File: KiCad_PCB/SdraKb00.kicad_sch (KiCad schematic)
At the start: 75 parts, among them J2 AVR-ISP-6, SW03 RotaryEncoder_Switch, SW1 Reset_SW, U2 PRTR5V0U2X, U3 ATmega32U4-A, Y1 16MHz

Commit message: First round assigning footprints.
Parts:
- C1, C10, C11, C12, C13, C14, C15, C16, C17, C18, C19, C2, C20, C3, C4, C5, C6, C7, C8, C9: footprint (none) -> Capacitor_SMD:C_0805_2012Metric_Pad1.18x1.45mm_HandSolder
- D00, D01, D02, D03, D10, D11, D12, D13, D20, D21, D22, D23: footprint (none) -> Diode_SMD:D_SOD-123
- D14, D15, D16, D17, D18, D4, D5, D6, D7, D8, D9: footprint LED_SMD:LED_SK6812MINI_PLCC4_3.5x3.5mm_P1.75mm -> (none)
- F1: footprint (none) -> Fuse:Fuse_1206_3216Metric_Pad1.42x1.75mm_HandSolder
- H1, H2, H3, H4: footprint (none) -> MountingHole:MountingHole_2mm
- J2: footprint (none) -> random-keyboard-parts:Reset_Pretty-Mask
- R1, R2, R3, R4, R5, R6, R7, R8, R9: footprint (none) -> Resistor_SMD:R_0805_2012Metric_Pad1.20x1.40mm_HandSolder
- SW1: footprint (none) -> Button_Switch_SMD:SW_SPST_SKQG_WithStem
- U2: footprint (none) -> random-keyboard-parts:SOT143B
- USB1: footprint (none) -> Type-C:HRO-TYPE-C-31-M-12-HandSoldering
- Y1: footprint (none) -> Crystal:Crystal_SMD_3225-4Pin_3.2x2.5mm_HandSoldering
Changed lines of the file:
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@@
 			)
 		)
-		(property "Footprint" "LED_SMD:LED_SK6812MINI_PLCC4_3.5x3.5mm_P1.75mm"
+		(property "Footprint" ""
 			(at 332.74 113.03 0)
 			(effects
@@
 			)
 		)
-		(property "Footprint" ""
+		(property "Footprint" "MountingHole:MountingHole_2mm"
 			(at 135.89 149.86 0)
 			(effects
@@
 			)
 		)
-		(property "Footprint" "LED_SMD:LED_SK6812MINI_PLCC4_3.5x3.5mm_P1.75mm"
+		(property "Footprint" ""
 			(at 332.74 44.45 0)
 			(effects
@@
 			)
 		)
-		(property "Footprint" ""
+		(property "Footprint" "MountingHole:MountingHole_2mm"
 			(at 135.89 162.56 0)
 			(effects
@@
 			)
 		)
-		(property "Footprint" "LED_SMD:LED_SK6812MINI_PLCC4_3.5x3.5mm_P1.75mm"
+		(property "Footprint" ""
 			(at 360.68 78.74 0)
 			(effects
@@
 			)
 		)
-		(property "Footprint" ""
+		(property "Footprint" "Capacitor_SMD:C_0805_2012Metric_Pad1.18x1.45mm_HandSolder"
 			(at 123.19 114.3 0)
 			(effects
@@
 			)
 		)
-		(property "Footprint" ""
+		(property "Footprint" "MountingHole:MountingHole_2mm"
 			(at 158.75 149.86 0)
 			(effects
@@
 			)
 		)
-		(property "Footprint" ""
+		(property "Footprint" "Capacitor_SMD:C_0805_2012Metric_Pad1.18x1.45mm_HandSolder"
 			(at 295.91 67.31 0)
 			(effects
@@
 			)
 		)
-		(property "Footprint" ""
+		(property "Footprint" "Capacitor_SMD:C_0805_2012Metric_Pad1.18x1.45mm_HandSolder"
 			(at 295.91 101.6 0)
 			(effects
@@
 			)
 		)
-		(property "Footprint" ""
+		(property "Footprint" "Diode_SMD:D_SOD-123"
 			(at 172.72 48.26 90)
 			(effects
@@
 			)
 		)
-		(property "Footprint" ""
+		(property "Footprint" "Diode_SMD:D_SOD-123"
 			(at 123.19 48.26 90)
 			(effects
@@
 			)
 		)
-		(property "Footprint" ""
+		(property "Footprint" "Resistor_SMD:R_0805_2012Metric_Pad1.20x1.40mm_HandSolder"
 			(at 204.47 40.64 0)
 			(effects
@@
 			)
 		)
-		(property "Footprint" ""
+		(property "Footprint" "random-keyboard-parts:SOT143B"
 			(at 90.17 175.26 0)
 			(effects
@@
 			)
 		)
-		(property "Footprint" ""
+		(property "Footprint" "Diode_SMD:D_SOD-123"
 			(at 123.19 88.9 90)
 			(effects
@@
 			)
 		)
-		(property "Footprint" ""
+		(property "Footprint" "Fuse:Fuse_1206_3216Metric_Pad1.42x1.75mm_HandSolder"
 			(at 91.44 149.86 0)
 			(effects
@@
 			)
 		)
-		(property "Footprint" ""
+		(property "Footprint" "Type-C:HRO-TYPE-C-31-M-12-HandSoldering"
 			(at 45.72 162.56 0)
 			(effects
@@
 			)
 		)
-		(property "Footprint" ""
+		(property "Footprint" "Capacitor_SMD:C_0805_2012Metric_Pad1.18x1.45mm_HandSolder"
 			(at 323.85 67.31 0)
 			(effects
@@
 			)
 		)
-		(property "Footprint" ""
+		(property "Footprint" "Diode_SMD:D_SOD-123"
 			(at 139.7 88.9 90)
 			(effects
@@
 			)
 		)
-		(property "Footprint" "LED_SMD:LED_SK6812MINI_PLCC4_3.5x3.5mm_P1.75mm"
+		(property "Footprint" ""
 			(at 360.68 113.03 0)
 			(effects
@@
 			)
 		)
-		(property "Footprint" ""
+		(property "Footprint" "Capacitor_SMD:C_0805_2012Metric_Pad1.18x1.45mm_HandSolder"
 			(at 267.97 33.02 0)
 			(effects
@@
 			)
 		)
-		(property "Footprint" ""
+		(property "Footprint" "Capacitor_SMD:C_0805_2012Metric_Pad1.18x1.45mm_HandSolder"
 			(at 267.97 67.31 0)
 			(effects
@@
 			)
 		)
-		(property "Footprint" "LED_SMD:LED_SK6812MINI_PLCC4_3.5x3.5mm_P1.75mm"
+		(property "Footprint" ""
 			(at 332.74 78.74 0)
 			(effects
@@
 			)
 		)
-		(property "Footprint" ""
+		(property "Footprint" "Capacitor_SMD:C_0805_2012Metric_Pad1.18x1.45mm_HandSolder"
 			(at 154.94 124.46 0)
 			(effects
@@
 			)
 		)
-		(property "Footprint" ""
+		(property "Footprint" "random-keyboard-parts:Reset_Pretty-Mask"
 			(at 201.93 119.38 90)
 			(effects
@@
 			)
 		)
-		(property "Footprint" "LED_SMD:LED_SK6812MINI_PLCC4_3.5x3.5mm_P1.75mm"
+		(property "Footprint" ""
 			(at 304.8 44.45 0)
 			(effects
@@
 			)
 		)
-		(property "Footprint" "LED_SMD:LED_SK6812MINI_PLCC4_3.5x3.5mm_P1.75mm"
+		(property "Footprint" ""
 			(at 276.86 78.74 0)
 			(effects
@@
 			)
 		)
-		(property "Footprint" ""
+		(property "Footprint" "Diode_SMD:D_SOD-123"
 			(at 172.72 88.9 90)
 			(effects
@@
 			)
 		)
-		(property "Footprint" "LED_SMD:LED_SK6812MINI_PLCC4_3.5x3.5mm_P1.75mm"
+		(property "Footprint" ""
 			(at 304.8 113.03 0)
 			(effects
@@
 			)
 		)
-		(property "Footprint" ""
+		(property "Footprint" "Capacitor_SMD:C_0805_2012Metric_Pad1.18x1.45mm_HandSolder"
 			(at 323.85 33.02 0)
 			(effects
@@
 			)
 		)
-		(property "Footprint" ""
+		(property "Footprint" "Capacitor_SMD:C_0805_2012Metric_Pad1.18x1.45mm_HandSolder"
 			(at 213.36 38.1 0)
 			(effects
@@
 			)
 		)
-		(property "Footprint" ""
+		(property "Footprint" "Capacitor_SMD:C_0805_2012Metric_Pad1.18x1.45mm_HandSolder"
 			(at 351.79 101.6 0)
 			(effects
@@
 			)
 		)
-		(property "Footprint" ""
+		(property "Footprint" "Resistor_SMD:R_0805_2012Metric_Pad1.20x1.40mm_HandSolder"
 			(at 204.47 156.21 0)
 			(effects
@@
 			)
 		)
-		(property "Footprint" ""
+		(property "Footprint" "Capacitor_SMD:C_0805_2012Metric_Pad1.18x1.45mm_HandSolder"
 			(at 100.33 114.3 0)
 			(effects
@@
 			)
 		)
-		(property "Footprint" ""
+		(property "Footprint" "Resistor_SMD:R_0805_2012Metric_Pad1.20x1.40mm_HandSolder"
 			(at 204.47 45.72 0)
 			(effects
@@
 			)
 		)
-		(property "Footprint" ""
+		(property "Footprint" "Capacitor_SMD:C_0805_2012Metric_Pad1.18x1.45mm_HandSolder"
 			(at 31.75 72.39 0)
 			(effects
@@
 			)
 		)
-		(property "Footprint" ""
+		(property "Footprint" "Capacitor_SMD:C_0805_2012Metric_Pad1.18x1.45mm_HandSolder"
 			(at 135.89 114.3 0)
 			(effects
@@
 			)
 		)
-		(property "Footprint" ""
+		(property "Footprint" "Diode_SMD:D_SOD-123"
 			(at 123.19 68.58 90)
 			(effects
@@
 			)
 		)
-		(property "Footprint" ""
+		(property "Footprint" "Capacitor_SMD:C_0805_2012Metric_Pad1.18x1.45mm_HandSolder"
 			(at 213.36 48.26 0)
 			(effects
@@
 			)
 		)
-		(property "Footprint" "LED_SMD:LED_SK6812MINI_PLCC4_3.5x3.5mm_P1.75mm"
+		(property "Footprint" ""
 			(at 304.8 78.74 0)
 			(effects
@@
 			)
 		)
-		(property "Footprint" ""
+		(property "Footprint" "Capacitor_SMD:C_0805_2012Metric_Pad1.18x1.45mm_HandSolder"
 			(at 351.79 67.31 0)
 			(effects
@@
 			)
 		)
-		(property "Footprint" ""
+		(property "Footprint" "Diode_SMD:D_SOD-123"
 			(at 139.7 48.26 90)
 			(effects
@@
 			)
 		)
-		(property "Footprint" ""
+		(property "Footprint" "Diode_SMD:D_SOD-123"
 			(at 156.21 88.9 90)
 			(effects
@@
 			)
 		)
-		(property "Footprint" ""
+		(property "Footprint" "Capacitor_SMD:C_0805_2012Metric_Pad1.18x1.45mm_HandSolder"
 			(at 111.76 114.3 0)
 			(effects
@@
 			)
 		)
-		(property "Footprint" ""
+		(property "Footprint" "Resistor_SMD:R_0805_2012Metric_Pad1.20x1.40mm_HandSolder"
 			(at 81.28 90.17 0)
 			(effects
@@
 			)
 		)
-		(property "Footprint" ""
+		(property "Footprint" "Capacitor_SMD:C_0805_2012Metric_Pad1.18x1.45mm_HandSolder"
 			(at 295.91 33.02 0)
 			(effects
@@
 			)
 		)
-		(property "Footprint" ""
+		(property "Footprint" "Resistor_SMD:R_0805_2012Metric_Pad1.20x1.40mm_HandSolder"
 			(at 66.04 173.99 0)
 			(effects
@@
 			)
 		)
-		(property "Footprint" "LED_SMD:LED_SK6812MINI_PLCC4_3.5x3.5mm_P1.75mm"
+		(property "Footprint" ""
 			(at 276.86 113.03 0)
 			(effects
@@
 			)
 		)
-		(property "Footprint" ""
+		(property "Footprint" "Resistor_SMD:R_0805_2012Metric_Pad1.20x1.40mm_HandSolder"
 			(at 104.14 163.83 0)
 			(effects
@@
 			)
 		)
-		(property "Footprint" ""
+		(property "Footprint" "Diode_SMD:D_SOD-123"
 			(at 172.72 68.58 90)
 			(effects
@@
 			)
 		)
-		(property "Footprint" "LED_SMD:LED_SK6812MINI_PLCC4_3.5x3.5mm_P1.75mm"
+		(property "Footprint" ""
 			(at 276.86 44.45 0)
 			(effects
@@
 			)
 		)
-		(property "Footprint" ""
+		(property "Footprint" "Crystal:Crystal_SMD_3225-4Pin_3.2x2.5mm_HandSoldering"
 			(at 163.83 120.65 0)
 			(effects
@@
 			)
 		)
-		(property "Footprint" ""
+		(property "Footprint" "Capacitor_SMD:C_0805_2012Metric_Pad1.18x1.45mm_HandSolder"
 			(at 171.45 124.46 0)
 			(effects
@@
 			)
 		)
-		(property "Footprint" ""
+		(property "Footprint" "Capacitor_SMD:C_0805_2012Metric_Pad1.18x1.45mm_HandSolder"
 			(at 323.85 101.6 0)
 			(effects
@@
 			)
 		)
-		(property "Footprint" ""
+		(property "Footprint" "Diode_SMD:D_SOD-123"
 			(at 139.7 68.58 90)
 			(effects
@@
 			)
 		)
-		(property "Footprint" ""
+		(property "Footprint" "Diode_SMD:D_SOD-123"
 			(at 156.21 68.58 90)
 			(effects
@@
 			)
 		)
-		(property "Footprint" ""
+		(property "Footprint" "Resistor_SMD:R_0805_2012Metric_Pad1.20x1.40mm_HandSolder"
 			(at 73.66 173.99 0)
 			(effects
@@
 			)
 		)
-		(property "Footprint" ""
+		(property "Footprint" "Capacitor_SMD:C_0805_2012Metric_Pad1.18x1.45mm_HandSolder"
 			(at 267.97 101.6 0)
 			(effects
@@
 			)
 		)
-		(property "Footprint" ""
+		(property "Footprint" "Resistor_SMD:R_0805_2012Metric_Pad1.20x1.40mm_HandSolder"
 			(at 104.14 166.37 0)
 			(effects
@@
 			)
 		)
-		(property "Footprint" ""
+		(property "Footprint" "Button_Switch_SMD:SW_SPST_SKQG_WithStem"
 			(at 196.85 156.21 0)
 			(effects
@@
 			)
 		)
-		(property "Footprint" ""
+		(property "Footprint" "Resistor_SMD:R_0805_2012Metric_Pad1.20x1.40mm_HandSolder"
 			(at 256.54 36.83 0)
 			(effects
@@
 			)
 		)
-		(property "Footprint" ""
+		(property "Footprint" "Diode_SMD:D_SOD-123"
 			(at 156.21 48.26 90)
 			(effects
@@
 			)
 		)
-		(property "Footprint" ""
+		(property "Footprint" "MountingHole:MountingHole_2mm"
 			(at 158.75 162.56 0)
 			(effects

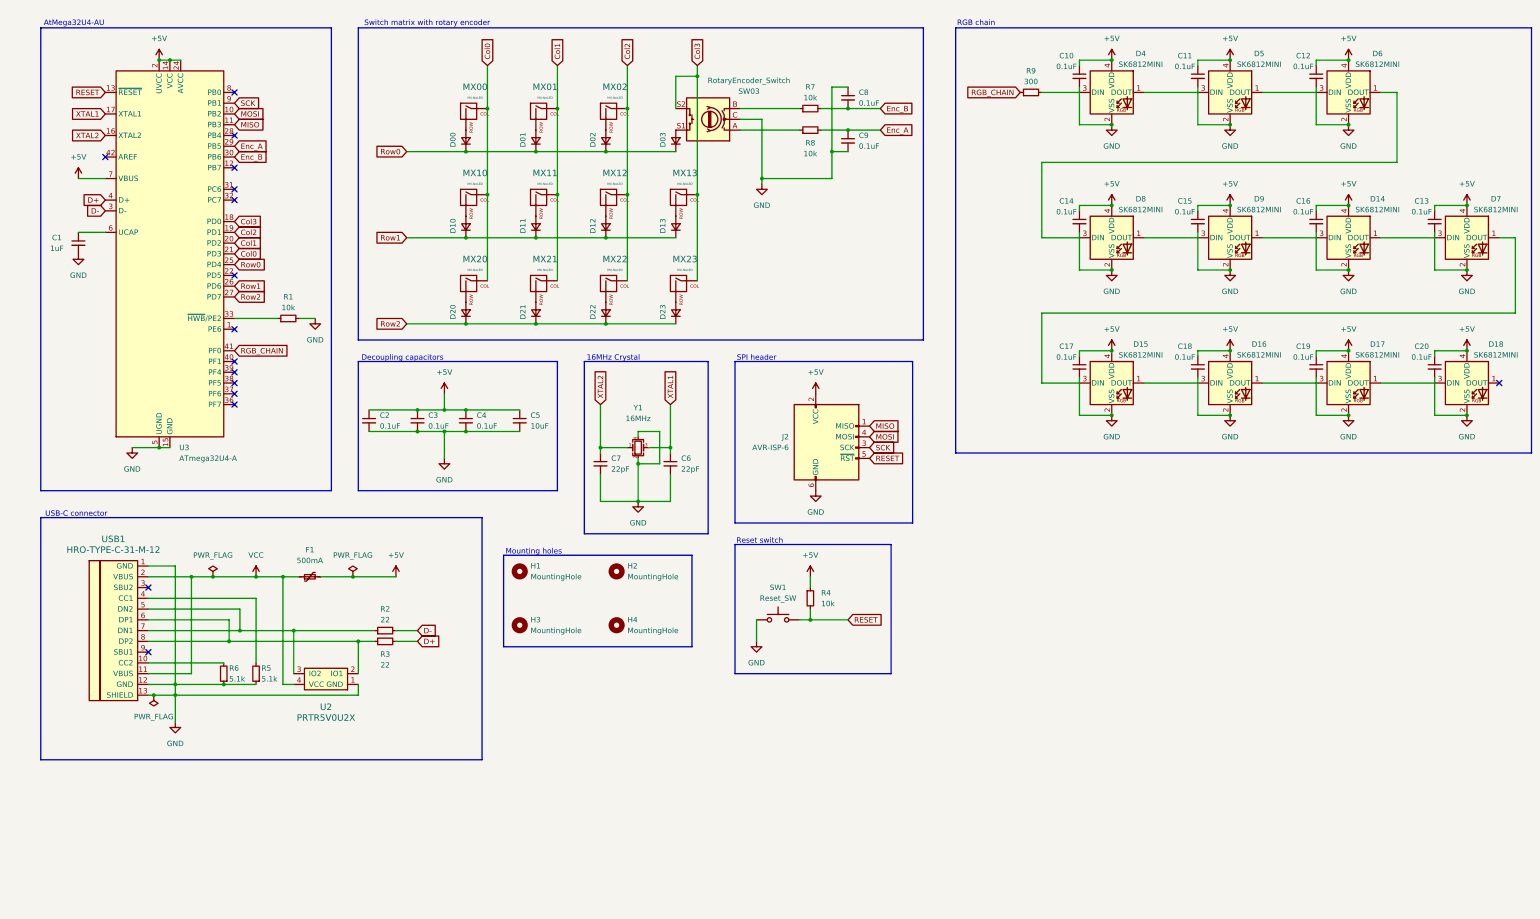
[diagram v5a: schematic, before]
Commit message: Complete footprint assignment.
- Removed unused submodules
- Adding marbastlib submodule
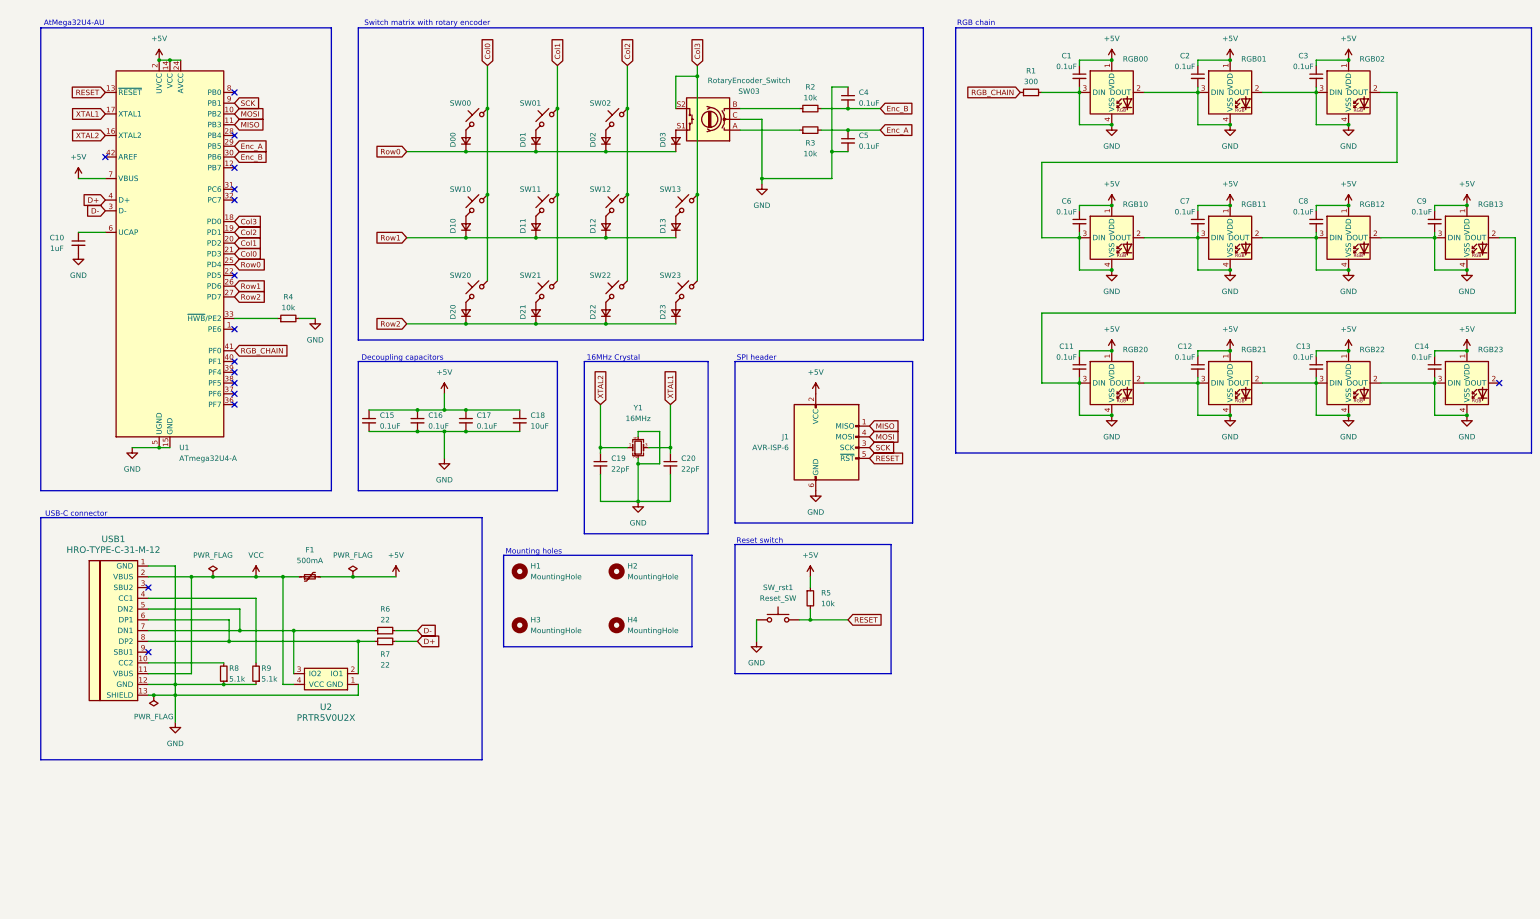
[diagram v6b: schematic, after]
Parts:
- removed D14, D15, D16, D17, D18, D4, D5, D6, D7, D8, D9: SK6812MINI, symbol LED:SK6812MINI
- removed MX00, MX01, MX02, MX10, MX11, MX12, MX13, MX20, MX21, MX22, MX23: MX-NoLED, symbol MX_Alps_Hybrid:MX-NoLED
- added RGB00, RGB01, RGB02, RGB10, RGB11, RGB12, RGB13, RGB20, RGB21, RGB22, RGB23: MX_SK6812MINI-E, marbastlib-mx:LED_MX_6028R, symbol marbastlib-mx:MX_SK6812MINI-E
- added SW00, SW01, SW02, SW10, SW11, SW12, SW13, SW20, SW21, SW22, SW23: SW_Push_45deg, marbastlib-mx:SW_MX_HS_CPG151101S11_1u, symbol Switch:SW_Push_45deg
- H1, H2, H3, H4: footprint MountingHole:MountingHole_2mm -> MountingHole:MountingHole_3.2mm_M3
- J1: renamed from J2; footprint random-keyboard-parts:Reset_Pretty-Mask -> Connector_IDC:IDC-Header_2x03_P2.54mm_Vertical
- SW03: footprint (none) -> marbastlib-various:ROT_Alps_EC11E-Switch
- U2: footprint random-keyboard-parts:SOT143B -> Package_TO_SOT_SMD:SOT-143_Handsoldering
- renumbered C10 to C1, C1 to C10, C17 to C11, C18 to C12, C19 to C13, C20 to C14, C2 to C15, C3 to C16, C4 to C17, C5 to C18, C7 to C19, C11 to C2, C6 to C20, C12 to C3, C8 to C4, C9 to C5, C14 to C6, C15 to C7, C16 to C8, C13 to C9, R9 to R1, R7 to R2, R8 to R3, R1 to R4, R4 to R5, R2 to R6, R3 to R7, R6 to R8, R5 to R9, SW1 to SW_rst1, U3 to U1
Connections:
- net +5V: now also RGB00.1 (VDD), RGB01.1 (VDD), RGB02.1 (VDD), RGB10.1 (VDD), RGB11.1 (VDD), RGB12.1 (VDD), RGB13.1 (VDD), RGB20.1 (VDD), RGB21.1 (VDD), RGB22.1 (VDD), RGB23.1 (VDD)
- net Col0: now also SW00.2, SW10.2, SW20.2
- net Col1: now also SW01.2, SW11.2, SW21.2
- net Col2: now also SW02.2, SW12.2, SW22.2
- net Col3: now also SW13.2, SW23.2
- net GND: now also R1.2, RGB00.2 (DOUT), RGB00.3 (DIN), RGB00.4 (VSS), RGB01.2 (DOUT), RGB01.3 (DIN), RGB01.4 (VSS), RGB02.2 (DOUT), RGB02.3 (DIN), RGB02.4 (VSS), RGB10.2 (DOUT), RGB10.3 (DIN), RGB10.4 (VSS), RGB11.2 (DOUT), RGB11.3 (DIN), RGB11.4 (VSS), RGB12.2 (DOUT), RGB12.3 (DIN), RGB12.4 (VSS), RGB13.2 (DOUT), RGB13.3 (DIN), RGB13.4 (VSS), RGB20.2 (DOUT), RGB20.3 (DIN), RGB20.4 (VSS), RGB21.2 (DOUT), RGB21.3 (DIN), RGB21.4 (VSS), RGB22.2 (DOUT), RGB22.3 (DIN), RGB22.4 (VSS), RGB23.3 (DIN), RGB23.4 (VSS)
- net at D11.2 (A): now also SW11.1
- net at D01.2 (A): now also SW01.1
- net at D21.2 (A): now also SW21.1
- net at D23.2 (A): now also SW23.1
- net at D00.2 (A): now also SW00.1
- net at D20.2 (A): now also SW20.1
- net at D12.2 (A): now also SW12.1
- net at D10.2 (A): now also SW10.1
- net at D22.2 (A): now also SW22.1
- net at D13.2 (A): now also SW13.1
- net at D02.2 (A): now also SW02.1

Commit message: Pcb design (#4)
* Aligning SWs, Ds, LEDs.

* Placing all components before routing.

* More wiring.

* More PCB routing.

* Routing MCU powerlines, Crystal ground zone.

* Finish routing power.

* Routing switch matrix.

* Cutting rounded corner edges.

* Improving silk screen placement.

* Finilizing PCB design.
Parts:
- J1: footprint Connector_IDC:IDC-Header_2x03_P2.54mm_Vertical -> Connector_PinHeader_2.00mm:PinHeader_1x06_P2.00mm_Horizontal
- RGB00, RGB01, RGB02, RGB10, RGB11, RGB12, RGB13, RGB20, RGB21, RGB22, RGB23: footprint marbastlib-mx:LED_MX_6028R -> marbastlib-mx:LED_MX_6028R-ROT
- renumbered C1 to Crgb00, C2 to Crgb01, C3 to Crgb02, C6 to Crgb10, C7 to Crgb11, C8 to Crgb12, C9 to Crgb13, C11 to Crgb20, C12 to Crgb21, C13 to Crgb22, C14 to Crgb23
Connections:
- net Col0: now also U1.41 (PF0); no longer U1.21 (PD3)
- net Col1: now also U1.40 (PF1); no longer U1.20 (PD2)
- net Col2: now also U1.39 (PF4); no longer U1.19 (PD1)
- net Col3: now also U1.38 (PF5); no longer U1.18 (PD0)
- net GND: no longer R1.2, RGB00.2 (DOUT), RGB00.3 (DIN), RGB01.2 (DOUT), RGB01.3 (DIN), RGB02.2 (DOUT), RGB02.3 (DIN), RGB10.2 (DOUT), RGB10.3 (DIN), RGB11.2 (DOUT), RGB11.3 (DIN), RGB12.2 (DOUT), RGB12.3 (DIN), RGB13.2 (DOUT), RGB13.3 (DIN), RGB20.2 (DOUT), RGB20.3 (DIN), RGB21.2 (DOUT), RGB21.3 (DIN), RGB22.2 (DOUT), RGB22.3 (DIN), RGB23.3 (DIN)
- net RGB_CHAIN: now also U1.8 (PB0); no longer U1.41 (PF0)
- net DN: now reaches R7.1, U2.2 (IO1), USB1.6 (DP1), USB1.8 (DP2)
- net DP: now reaches R6.1, U2.3 (IO2), USB1.5 (DN2), USB1.7 (DN1)
- new net: RGB10.2 (DOUT), RGB11.3 (DIN)
- new net: RGB02.2 (DOUT), RGB10.3 (DIN)
- new net: RGB00.2 (DOUT), RGB01.3 (DIN)
- new net: R1.2, RGB00.3 (DIN)
- new net: RGB22.2 (DOUT), RGB23.3 (DIN)
- new net: RGB21.2 (DOUT), RGB22.3 (DIN)
- new net: RGB11.2 (DOUT), RGB12.3 (DIN)
- new net: RGB12.2 (DOUT), RGB13.3 (DIN)
- new net: RGB13.2 (DOUT), RGB20.3 (DIN)
- new net: RGB01.2 (DOUT), RGB02.3 (DIN)
- new net: RGB20.2 (DOUT), RGB21.3 (DIN)

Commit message: Adding power indicator LED.
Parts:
- added D4: RED 1.8V, LED_SMD:LED_1206_3216Metric_Pad1.42x1.75mm_HandSolder, symbol Device:LED
- added R10: 640, Resistor_SMD:R_0805_2012Metric_Pad1.20x1.40mm_HandSolder, symbol Device:R
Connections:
- net +5V: now also R10.1
- net GND: now also D4.1 (K)
- net STATUS_LED: now reaches U1.36 (PF7)
- new net: D4.2 (A), R10.2
- no-connect marks 16 -> 15
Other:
- note added: "Power indicator"
